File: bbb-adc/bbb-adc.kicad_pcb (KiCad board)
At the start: 2 copper layers, 65.5 x 79 mm, 23 parts, among them P1 CONN_01X03, P2 CONN_01X02, P9 CONN_02X03, U1 ref5050, p8 CONN_02X23

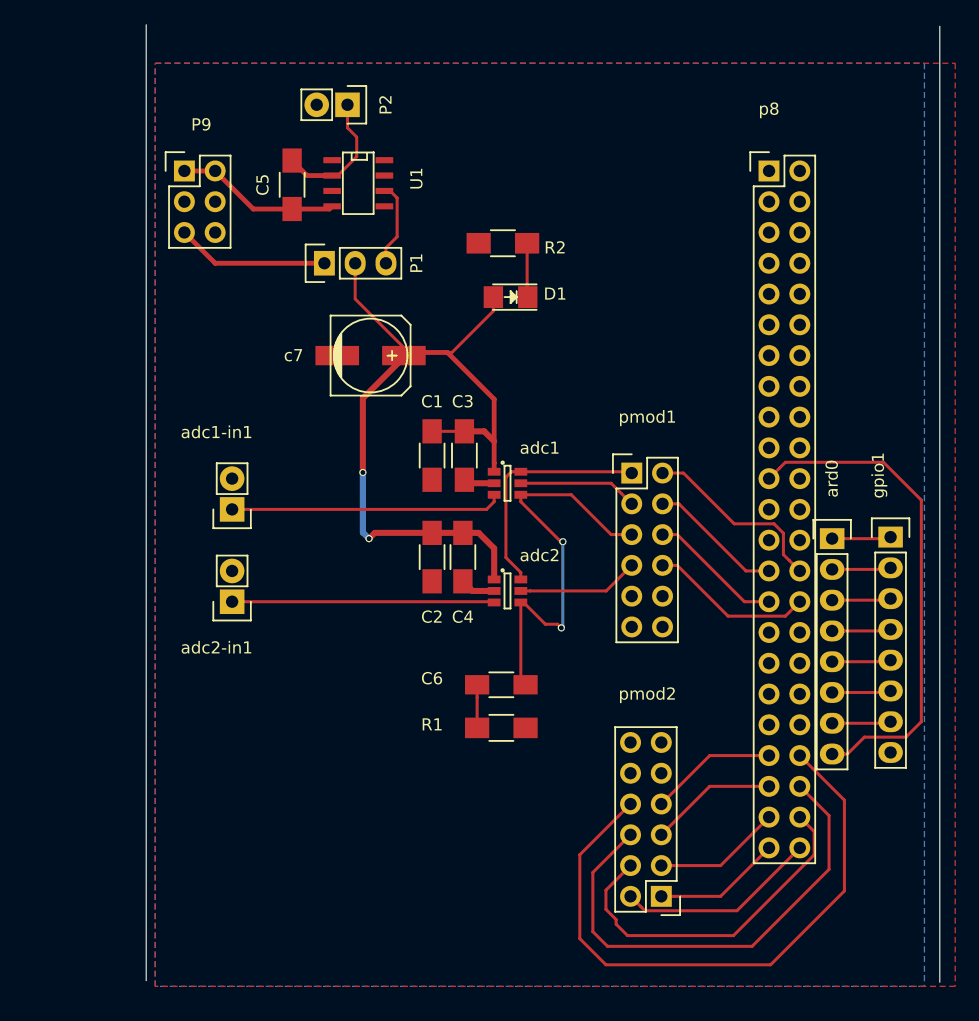
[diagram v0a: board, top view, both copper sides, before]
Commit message: inc track width, connect extra bbb to gpio, via size and ground stitching
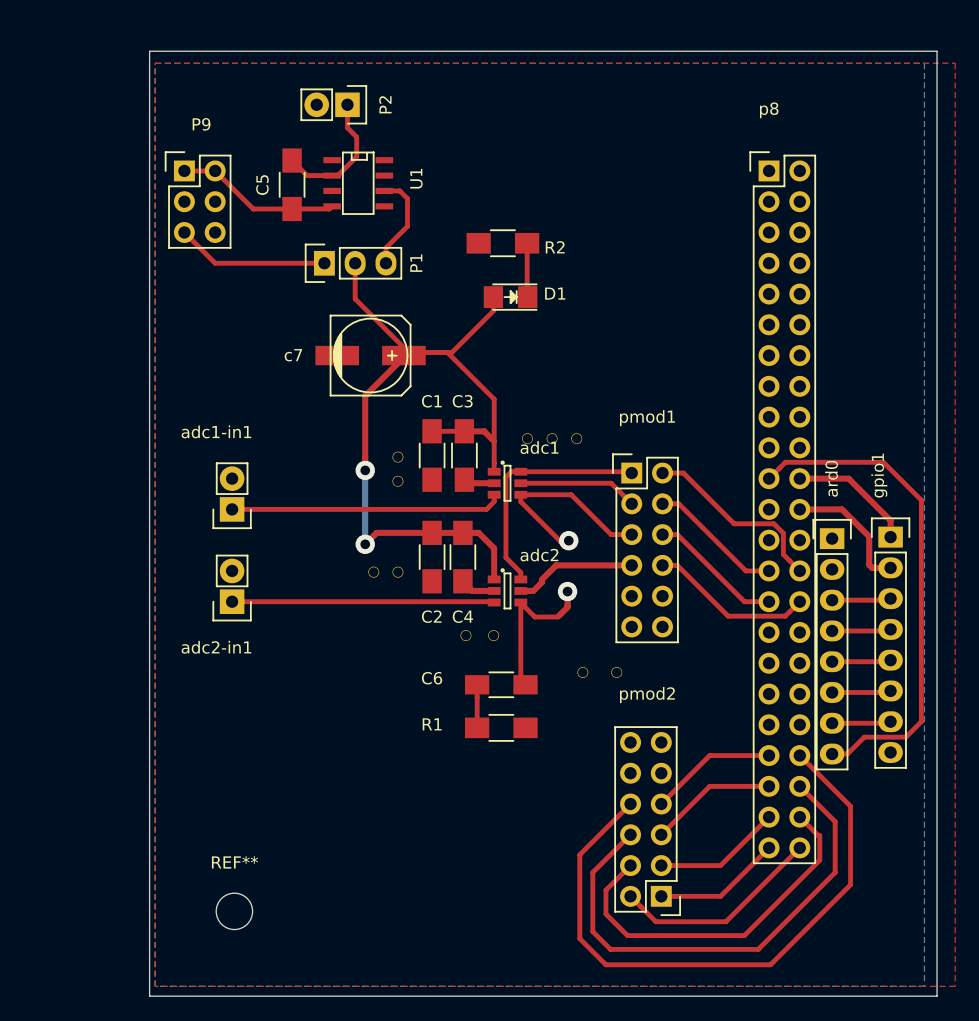
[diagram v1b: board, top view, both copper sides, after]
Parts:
- added REF**: via, via, F.Cu at (142.5, 89.0)
- added REF**: via, via, F.Cu at (157.2, 78.0)
- added REF**: via, via, F.Cu at (155.2, 78.0)
- added REF**: MountingHole_3mm, Mounting_Holes:MountingHole_3mm, F.Cu at (131.0, 117.0)
- added REF**: via, via, F.Cu at (144.5, 89.0)
- added REF**: via, via, F.Cu at (144.5, 79.5)
- added REF**: via, via, F.Cu at (144.5, 81.5)
- added REF**: via, via, F.Cu at (162.6, 97.3)
- added REF**: via, via, F.Cu at (159.8, 97.3)
- added REF**: via, via, F.Cu at (150.1, 94.2)
- added REF**: via, via, F.Cu at (152.4, 94.2)
- added REF**: via, via, F.Cu at (159.3, 78.0)
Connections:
- ard0 pad 1: Net-(ard0-Pad1) -> (no net)
- ard0 pad 2: Net-(ard0-Pad2) -> (no net)
- gpio1 pad 1: Net-(ard0-Pad1) -> gpio1
- gpio1 pad 2: Net-(ard0-Pad2) -> gpio2
- p8 pad 22: (no net) -> gpio1
- p8 pad 24: (no net) -> gpio2
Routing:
- net gpio2: track 0.00 -> 11.0 mm
- net gpio1: track 0.00 -> 10.5 mm
- net Net-(ard0-Pad1): track 4.88 -> 0.00 mm
- net Net-(ard0-Pad2): track 4.88 -> 0.00 mm
- net adc-clk: track 34.3 -> 29.6 mm
- net ref-5v: track 7.06 -> 8.24 mm
- net /bit5: track 39.8 -> 40.9 mm
- net /bit3: track 29.1 -> 30.1 mm
- net /bit1: track 16.6 -> 17.4 mm
- net adc-5v: track 68.6 -> 69.3 mm
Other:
- board size 65.5 x 79 mm -> 65 x 78 mm
- net class Default: trace_width 0.25 -> 0.5; via_dia 0.6 -> 1.6; via_drill 0.4 -> 0.8

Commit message: fab to oshpark
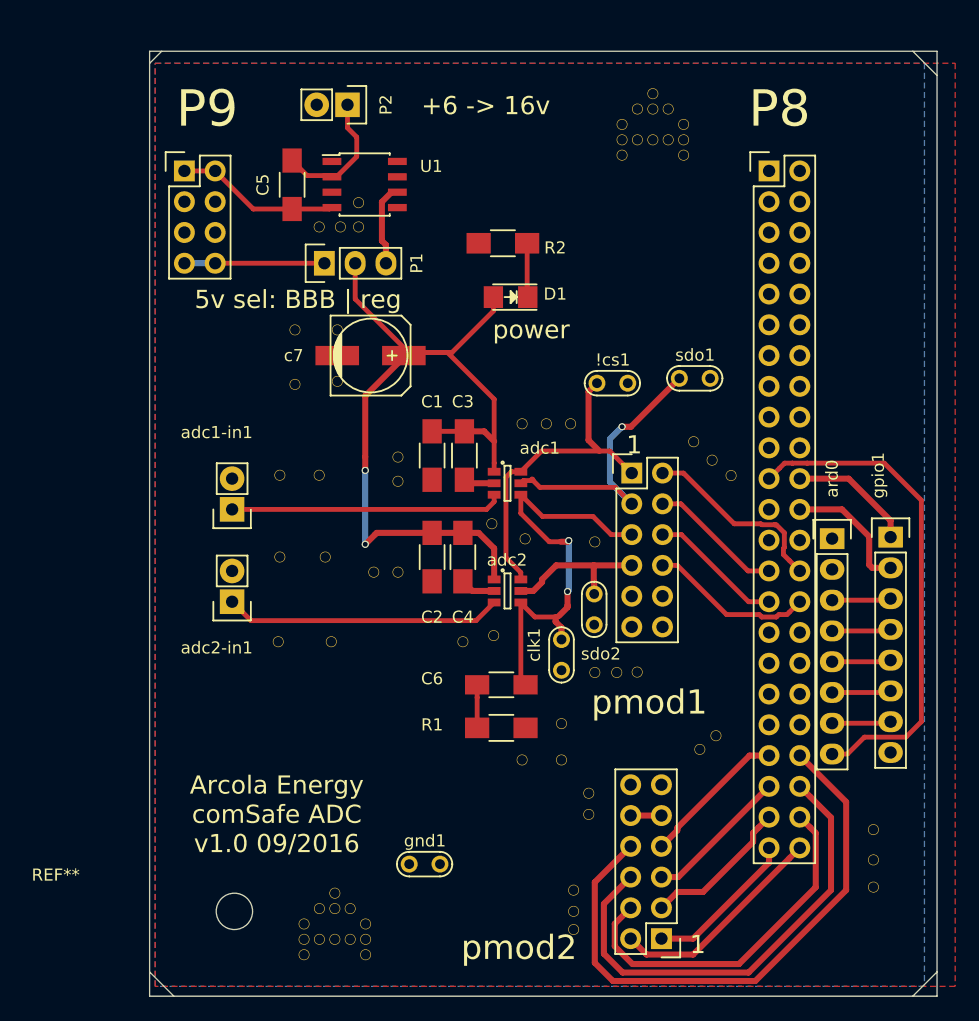
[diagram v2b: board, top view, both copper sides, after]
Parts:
- added !cs1: TEST, Measurement_Points:Test_Point, F.Cu at (162.2, 73.4)
- added REF**: via, via, F.Cu at (168.9, 78.2)
- added REF**: via, via, F.Cu at (136.0, 69.0)
- added REF**: via, via, F.Cu at (158.0, 101.5)
- added REF**: via, via, F.Cu at (158.0, 104.5)
- added REF**: via, via, F.Cu at (154.8, 104.5)
- added REF**: via, via, F.Cu at (159.0, 118.5)
- added REF**: via, via, F.Cu at (159.0, 117.0)
- added REF**: via, via, F.Cu at (159.0, 115.2)
- added REF**: via, via, F.Cu at (139.0, 94.7)
- added REF**: via, via, F.Cu at (134.6, 94.7)
- added REF**: via, via, F.Cu at (138.5, 87.8)
- added REF**: via, via, F.Cu at (170.4, 79.8)
- added REF**: via, via, F.Cu at (134.8, 87.8)
- added REF**: via, via, F.Cu at (138.0, 81.0)
- added REF**: via, via, F.Cu at (134.8, 81.0)
- added REF**: via, via, F.Cu at (183.8, 115.0)
- added REF**: via, via, F.Cu at (183.8, 112.8)
- added REF**: via, via, F.Cu at (183.8, 110.2)
- added REF**: via, via, F.Cu at (160.2, 107.2)
- added REF**: via, via, F.Cu at (160.2, 109.0)
- added REF**: via, via, F.Cu at (169.4, 103.6)
- added REF**: via, via, F.Cu at (170.8, 102.5)
- added REF**: via, via, F.Cu at (141.2, 58.5)
- added REF**: via, via, F.Cu at (164.2, 97.2)
- added REF**: via, via, F.Cu at (172.0, 81.0)
- added REF**: via, via, F.Cu at (152.2, 85.0)
- added REF**: via, via, F.Cu at (155.0, 86.2)
- added REF**: via, via, F.Cu at (160.8, 86.5)
- added REF**: via, via, F.Cu at (141.2, 60.5)
- added REF**: via, via, F.Cu at (139.8, 60.5)
- added REF**: via, via, F.Cu at (138.0, 60.5)
- added REF**: via, via, F.Cu at (139.5, 69.0)
- added REF**: via, via, F.Cu at (139.5, 73.2)
- added REF**: via, via, F.Cu at (136.0, 73.5)
- added REF**11: via, via, F.Cu at (163.0, 52.0)
- added REF**11: via, via, F.Cu at (136.8, 118.0)
- added REF**15: via, via, F.Cu at (168.1, 52.0)
- added REF**15: via, via, F.Cu at (141.8, 118.0)
- added REF**16: via, via, F.Cu at (163.0, 53.3)
- added REF**16: via, via, F.Cu at (136.8, 119.3)
- added REF**17: via, via, F.Cu at (164.3, 53.3)
- added REF**17: via, via, F.Cu at (138.0, 119.3)
- added REF**18: via, via, F.Cu at (165.5, 53.3)
- added REF**18: via, via, F.Cu at (139.3, 119.3)
- added REF**19: via, via, F.Cu at (166.8, 53.3)
- added REF**19: via, via, F.Cu at (140.6, 119.3)
- added REF**20: via, via, F.Cu at (168.1, 53.3)
- added REF**20: via, via, F.Cu at (141.8, 119.3)
- added REF**21: via, via, F.Cu at (163.0, 54.6)
- added REF**21: via, via, F.Cu at (136.8, 120.6)
- added REF**25: via, via, F.Cu at (168.1, 54.6)
- added REF**25: via, via, F.Cu at (141.8, 120.6)
- added REF**3: via, via, F.Cu at (165.5, 49.5)
- added REF**3: via, via, F.Cu at (139.3, 115.5)
- added REF**7: via, via, F.Cu at (164.3, 50.8)
- added REF**7: via, via, F.Cu at (138.0, 116.8)
- added REF**8: via, via, F.Cu at (165.5, 50.8)
- added REF**8: via, via, F.Cu at (139.3, 116.8)
- added REF**9: via, via, F.Cu at (166.8, 50.8)
- added REF**9: via, via, F.Cu at (140.6, 116.8)
- added clk1: TEST, Measurement_Points:Test_Point, F.Cu at (158.0, 95.8)
- added gnd1: TEST, Measurement_Points:Test_Point, F.Cu at (146.7, 113.1)
- added sdo1: TEST, Measurement_Points:Test_Point, F.Cu at (169.0, 73.0)
- added sdo2: TEST, Measurement_Points:Test_Point, F.Cu at (160.7, 92.1)
- P9: value CONN_02X03 -> CONN_02X04; footprint Pin_Headers:Pin_Header_Straight_2x03 -> Pin_Headers:Pin_Header_Straight_2x04
- U1: footprint fp:SOIC-8-N -> Housings_SOIC:SOIC-8_3.9x4.9mm_Pitch1.27mm
- moved pmod2 3.49 mm to (166.2, 119.2)
- moved REF** 1.33 mm to (158.8, 76.8)
- moved REF** 1.32 mm to (156.8, 76.8)
- moved REF** 1.31 mm to (154.8, 76.8)
- moved REF** 0.98 mm to (160.8, 97.3)
- moved REF** 0.57 mm to (149.9, 94.7)
- moved U1 0.50 mm to (141.8, 57.0), turned to 0 degrees
- renumbered p8 to P8
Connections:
- P9 pad 5: bbb-5v -> (no net)
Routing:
- net adc1-sdo: track 9.86 -> 24.1 mm, vias 0 -> 1
- net adc-cs: track 19.6 -> 27.2 mm
- net adc-clk: track 29.6 -> 36.5 mm
- net /bit7: track 51.2 -> 48.0 mm
- net Earth: track 19.1 -> 21.6 mm
- net adc2-sdo: track 10.2 -> 12.5 mm
- net /bit0: track 10.5 -> 12.7 mm
- net /bit2: track 10.5 -> 12.4 mm
- net /bit5: track 40.9 -> 39.1 mm
- net /bit6: track 10.5 -> 12.1 mm
- net /bit4: track 10.5 -> 12.0 mm
- net Net-(adc2-Pad3): track 21.7 -> 22.9 mm
- net bbb-5v: track 12.6 -> 11.6 mm
- net /bit1: track 17.4 -> 18.2 mm
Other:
- outline, holes or cut-outs redrawn
- net class Default: via_dia 1.6 -> 0.6; via_drill 0.8 -> 0.4
- board text added: "+6 -> 16v"
- board text added: "1"
- board text added: "5v sel: BBB | reg"
- board text added: "Arcola Energy comSafe ADC v1.0 09/2016"
- board text added: "power"

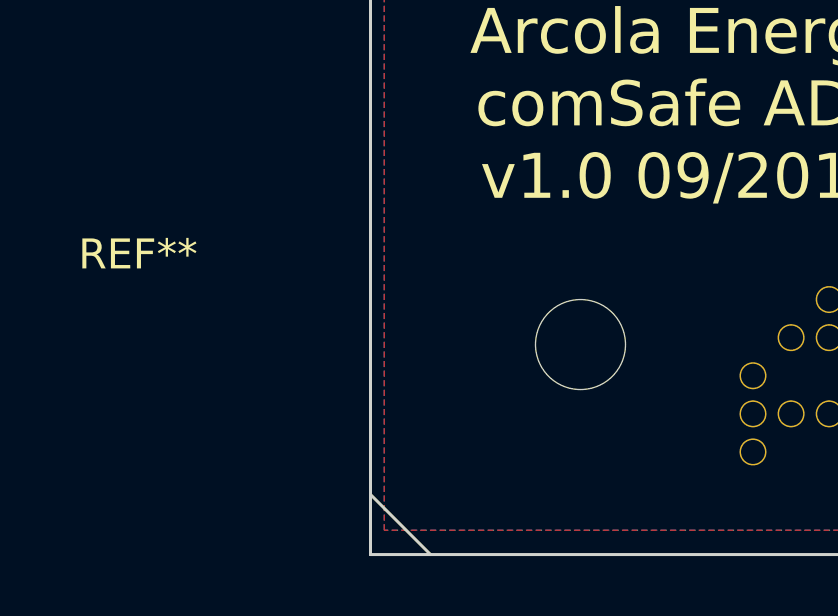
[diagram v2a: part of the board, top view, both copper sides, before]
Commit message: added farnell #;
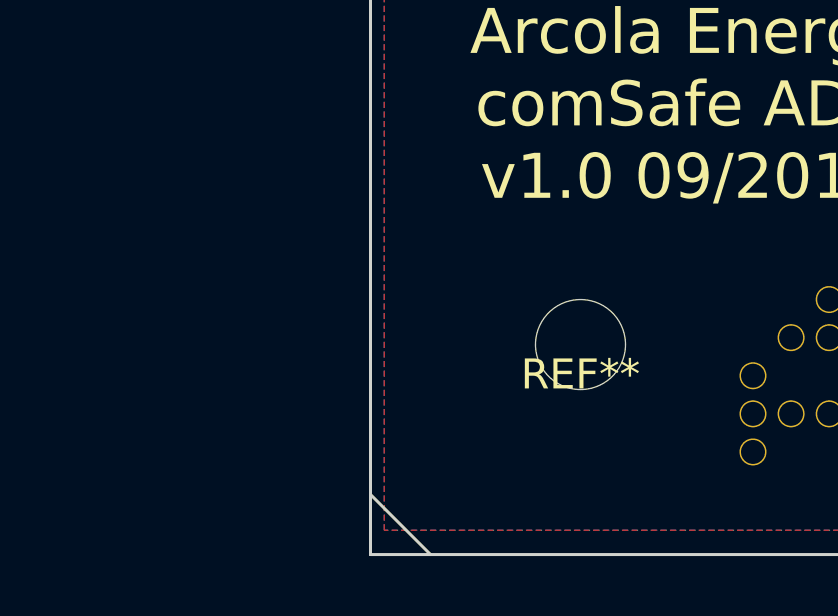
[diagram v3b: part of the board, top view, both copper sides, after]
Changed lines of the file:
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@@
 (kicad_pcb (version 4) (host pcbnew "(2015-06-25 BZR 5821)-product")
   (general
-    (links 157)
+    (links 147)
     (no_connects 4)
-    (area 113.832143 45.949999 190.500001 124.050001)
+    (area 121.764667 45.949999 190.500001 124.050001)
     (thickness 1.6)
     (drawings 14)
@@
     (descr "Mounting hole, Befestigungsbohrung, 3mm, No Annular, Kein Restring,")
     (tags "Mounting hole, Befestigungsbohrung, 3mm, No Annular, Kein Restring,")
-    (fp_text reference REF** (at -14.75 -3) (layer F.SilkS)
-      (effects (font (size 1 1) (thickness 0.15)))
-    )
+    (fp_text reference REF** (at 0 1) (layer F.SilkS)
+      (effects (font (size 1 1) (thickness 0.15)))
+    )
